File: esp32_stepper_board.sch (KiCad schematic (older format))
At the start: 35 parts, among them J1 Micro_SD_Card, J10 Endstop C/Z, J11 Aux1_I2C, J12 IO0_IO2_JP, J2 Aux2_GPIO, J3 DC_PWR, J4 Servo, J5 Stepper A/X, J6 Stepper B/Y, J7 Stepper C/Y, J8 Endstop A/X, J9 Endstop B/Y, SW1 Rotary_Encoder_Switch, U1 LM1117-5.0, U2 STEPSTICK, U3 ESP-DEVKITC, U4 STEPSTICK, U5 STEPSTICK, U6 OLED_I2C, U7 PCF8574

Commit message: Test board and components
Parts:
- removed C1: 100n, Capacitors_SMD:C_0805, symbol C
- removed J1: Micro_SD_Card, Connect:microSD_Card_Receptacle_Wuerth_693072010801, symbol Micro_SD_Card
- removed R2, R3, R4, R5, R6: 10k, Resistors_SMD:R_0805, symbol R
- removed SW1: Rotary_Encoder_Switch, symbol Rotary_Encoder_Switch
- added SW1: SW_DIP_x01, custom:SlideSw, symbol SW_DIP_x01
- added U3: lc_tech_sd_module, custom:lc_tech_sd_module, symbol lc_tech_sd_module
- added U7: rotary_enc_module, custom:ky-040-rotary-encoder-module, symbol rotary_enc_module
- C1: renamed from C2; footprint (none) -> Capacitors_ThroughHole:CP_Radial_D8.0mm_P2.50mm
- C2: renamed from C3; footprint (none) -> Capacitors_ThroughHole:CP_Radial_D8.0mm_P2.50mm
- C3: renamed from C4; footprint Capacitors_SMD:CP_Elec_6.3x7.7 -> custom:C_Radial_lying_flat_D8_L11_P2.5
- C4: renamed from C5; footprint Capacitors_SMD:CP_Elec_6.3x7.7 -> custom:C_Radial_lying_flat_D8_L11_P2.5
- C5: renamed from C6; footprint Capacitors_SMD:CP_Elec_6.3x7.7 -> custom:C_Radial_lying_flat_D8_L11_P2.5
- C6: renamed from C7; footprint Capacitors_SMD:C_0805 -> Capacitors_ThroughHole:C_Disc_D4.3mm_W1.9mm_P5.00mm
- J11: renamed from J12; footprint (none) -> Pin_Headers:Pin_Header_Straight_1x02_Pitch2.54mm
- R1: footprint Resistors_SMD:R_0805 -> Resistors_ThroughHole:R_Axial_DIN0204_L3.6mm_D1.6mm_P1.90mm_Vertical
- R2: renamed from R7; footprint Resistors_SMD:R_0805 -> Resistors_ThroughHole:R_Axial_DIN0204_L3.6mm_D1.6mm_P1.90mm_Vertical
- R3: renamed from R8; footprint Resistors_SMD:R_0805 -> Resistors_ThroughHole:R_Axial_DIN0204_L3.6mm_D1.6mm_P1.90mm_Vertical
- U1: footprint (none) -> TO_SOT_Packages_THT:TO-220-3_Vertical
- U4: renamed from U3; footprint (none) -> custom:DEVKITC
- U8: renamed from U6; footprint (none) -> custom:ssd1306_oled_0.96in
- U9: renamed from U7; footprint Housings_SOIC:SOIC-16_3.9x9.9mm_Pitch1.27mm -> Housings_DIP:DIP-16_W7.62mm
- renumbered J2 to J1, J11 to J10, J3 to J2, J4 to J3, J5 to J4, J6 to J5, J7 to J6, J8 to J7, J9 to J8, J10 to J9, U4 to U5, U5 to U6
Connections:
- net 12v: now also SW1.2; no longer J2.1
- net 3v3: now also U3.1 (3v3), U7.4 (Vin)
- net GND: now also U3.6 (GND), U7.5 (GND)
- net RENC_CLK: now also U7.1 (CLK)
- net RENC_DT: now also U7.2 (DT)
- net SD_MISO: now also U3.5 (MISO)
- net SD_MOSI: now also U3.3 (MOSI)
- net SD_SCK: now also U3.4 (CLK); no longer R1.2
- net ~RENC_SW: now also U7.3 (SW)
- new net: R1.2, U3.2 (CS)
- new net Vin: J2.1, SW1.1
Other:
- moved on the sheet: C1, C2, R1, U1, U4

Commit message: fix silk screen label for c/z stepper
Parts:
- J6: value Stepper C/Y -> Stepper C/Z
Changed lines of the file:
@@
 P 3150 10450
 F 0 "J6" H 3150 10650 50  0000 C CNN
-F 1 "Stepper C/Y" V 3250 10400 50  0000 C CNN
+F 1 "Stepper C/Z" V 3250 10400 50  0000 C CNN
 F 2 "Connectors_JST:JST_PH_B4B-PH-K_04x2.00mm_Straight" H 3150 10450 50  0001 C CNN
 F 3 "" H 3150 10450 50  0001 C CNN

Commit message: Fixed devkit footprint and rerouted board
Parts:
- removed J1: Aux2_GPIO, Connectors_JST:JST_PH_B12B-PH-K_12x2.00mm_Straight, symbol Conn_02x06_Odd_Even
- added J1: AUX_2A_GPIO_LN, Connectors_JST:JST_PH_B6B-PH-K_06x2.00mm_Straight, symbol Conn_01x06
- added J12: PWRSEL_2A, Pin_Headers:Pin_Header_Straight_1x03_Pitch2.54mm, symbol Conn_01x03
- added J13: AUX_2B_GPIO_HN, Connectors_JST:JST_PH_B6B-PH-K_06x2.00mm_Straight, symbol Conn_01x06
- added J14: PWRSEL_2B, Pin_Headers:Pin_Header_Straight_1x03_Pitch2.54mm, symbol Conn_01x03
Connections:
- net labels added: PWR1, PWR2
- wire segments 178 -> 184
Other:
- moved on the sheet: J10, J11, J2
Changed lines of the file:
@@
 LIBS:valves
 LIBS:custom
-LIBS:custom_parts
 LIBS:esp32_stepper_board-cache
 EELAYER 25 0
@@
 L Jack-DC J2
 U 1 1 5A64C62C
-P 7800 10300
-F 0 "J2" H 7800 10510 50  0000 C CNN
-F 1 "DC_PWR" H 7800 10125 50  0000 C CNN
-F 2 "Connect:BARREL_JACK" H 7850 10260 50  0001 C CNN
-F 3 "" H 7850 10260 50  0001 C CNN
-	1    7800 10300
-	1    0    0    -1
-$EndComp
-Text Label 8450 10400 2    60   ~ 0
-GND
-Text Label 8450 10200 2    60   ~ 0
+P 8150 10300
+F 0 "J2" H 8150 10510 50  0000 C CNN
+F 1 "DC_PWR" H 8150 10125 50  0000 C CNN
+F 2 "Connect:BARREL_JACK" H 8200 10260 50  0001 C CNN
+F 3 "" H 8200 10260 50  0001 C CNN
+	1    8150 10300
+	1    0    0    -1
+$EndComp
+Text Label 8800 10400 2    60   ~ 0
+GND
+Text Label 8800 10200 2    60   ~ 0
 Vin
 $Comp
@@
 Text Label 5000 3350 0    60   ~ 0
 RENC_DT
-$Comp
-L Conn_02x06_Odd_Even J1
-U 1 1 5AA0C7C0
-P 6500 10150
-F 0 "J1" H 6550 10450 50  0000 C CNN
-F 1 "Aux2_GPIO" H 6550 9750 50  0000 C CNN
-F 2 "Connectors_JST:JST_PH_B12B-PH-K_12x2.00mm_Straight" H 6500 10150 50  0001 C CNN
-F 3 "" H 6500 10150 50  0001 C CNN
-	1    6500 10150
-	1    0    0    -1
-$EndComp
-Text Label 7200 10150 2    60   ~ 0
-GND
-Text Label 5900 10250 0    60   ~ 0
-GND
-Text Label 7200 10250 2    60   ~ 0
-3v3
-Text Label 5900 10150 0    60   ~ 0
+Text Label 7000 9850 3    60   ~ 0
+GND
+Text Label 7600 9850 3    60   ~ 0
+3v3
+Text Label 6550 9850 3    60   ~ 0
 5v
 Text Label 4200 6750 2    60   ~ 0
@@
 Text Label 4200 7450 2    60   ~ 0
 GPIO_EX7
-Text Label 5900 9950 0    60   ~ 0
+Text Label 5800 9850 3    60   ~ 0
 GPIO_EX0
-Text Label 7200 9950 2    60   ~ 0
+Text Label 5900 9850 3    60   ~ 0
 GPIO_EX1
-Text Label 5900 10050 0    60   ~ 0
+Text Label 6000 9850 3    60   ~ 0
 GPIO_EX2
-Text Label 7200 10050 2    60   ~ 0
+Text Label 6100 9850 3    60   ~ 0
 GPIO_EX3
-Text Label 5900 10350 0    60   ~ 0
+Text Label 7100 9850 3    60   ~ 0
 GPIO_EX4
-Text Label 7200 10350 2    60   ~ 0
+Text Label 7200 9850 3    60   ~ 0
 GPIO_EX5
-Text Label 5900 10450 0    60   ~ 0
+Text Label 7300 9850 3    60   ~ 0
 GPIO_EX6
-Text Label 7200 10450 2    60   ~ 0
+Text Label 7400 9850 3    60   ~ 0
 GPIO_EX7
 $Comp
 L Conn_01x04 J10
 U 1 1 5AA0F0CE
-P 5300 10450
-F 0 "J10" H 5300 10650 50  0000 C CNN
-F 1 "Aux1_I2C" V 5400 10400 50  0000 C CNN
-F 2 "Connectors_JST:JST_PH_B4B-PH-K_04x2.00mm_Straight" H 5300 10450 50  0001 C CNN
-F 3 "" H 5300 10450 50  0001 C CNN
-	1    5300 10450
-	0    1    1    0
-$EndComp
-Text Label 5400 9950 3    60   ~ 0
-GND
+P 5200 10450
+F 0 "J10" H 5200 10650 50  0000 C CNN
+F 1 "Aux1_I2C" V 5300 10400 50  0000 C CNN
+F 2 "Connectors_JST:JST_PH_B4B-PH-K_04x2.00mm_Straight" H 5200 10450 50  0001 C CNN
+F 3 "" H 5200 10450 50  0001 C CNN
+	1    5200 10450
+	0    1    1    0
+$EndComp
+Text Label 5300 9950 3    60   ~ 0
+GND
+Text Label 5100 9950 3    60   ~ 0
+3v3
 Text Label 5200 9950 3    60   ~ 0
-3v3
-Text Label 5300 9950 3    60   ~ 0
 SDA1
-Text Label 5100 9950 3    60   ~ 0
+Text Label 5000 9950 3    60   ~ 0
 SCL1
 $Comp
@@
 L Conn_01x02 J11
 U 1 1 5AA42D41
-P 8950 10450
-F 0 "J11" H 8950 10550 50  0000 C CNN
-F 1 "IO0_IO2_JP" V 9050 10400 50  0000 C CNN
-F 2 "Pin_Headers:Pin_Header_Straight_1x02_Pitch2.54mm" H 8950 10450 50  0001 C CNN
-F 3 "" H 8950 10450 50  0001 C CNN
-	1    8950 10450
-	0    1    1    0
-$EndComp
-Text Label 8850 9900 3    60   ~ 0
+P 9100 10450
+F 0 "J11" H 9100 10550 50  0000 C CNN
+F 1 "IO0_IO2_JP" V 9200 10400 50  0000 C CNN
+F 2 "Pin_Headers:Pin_Header_Straight_1x02_Pitch2.54mm" H 9100 10450 50  0001 C CNN
+F 3 "" H 9100 10450 50  0001 C CNN
+	1    9100 10450
+	0    1    1    0
+$EndComp
+Text Label 9000 9900 3    60   ~ 0
 IO0
-Text Label 8950 9900 3    60   ~ 0
+Text Label 9100 9900 3    60   ~ 0
 SD_MOSI
 $Comp
@@
 	3250 9950 3250 10250
 Wire Wire Line
-	8100 10400 8450 10400
-Wire Wire Line
-	8100 10200 8450 10200
+	8450 10400 8800 10400
+Wire Wire Line
+	8450 10200 8800 10200
 Wire Wire Line
 	6200 6950 5800 6950
@@
 	5500 2450 5000 2450
 Wire Wire Line
-	6300 9950 5900 9950
-Wire Wire Line
-	6800 9950 7200 9950
-Wire Wire Line
-	6300 10050 5900 10050
-Wire Wire Line
-	6300 10150 5900 10150
-Wire Wire Line
-	6300 10250 5900 10250
-Wire Wire Line
-	6300 10350 5900 10350
-Wire Wire Line
-	6300 10450 5900 10450
-Wire Wire Line
-	6800 10050 7200 10050
-Wire Wire Line
-	6800 10150 7200 10150
-Wire Wire Line
-	6800 10250 7200 10250
-Wire Wire Line
-	6800 10350 7200 10350
-Wire Wire Line
-	6800 10450 7200 10450
-Wire Wire Line
-	5400 10250 5400 9950
-Wire Wire Line
 	5300 10250 5300 9950
 Wire Wire Line
@@
 Wire Wire Line
 	5100 10250 5100 9950
+Wire Wire Line
+	5000 10250 5000 9950
 Wire Notes Line
 	10150 5600 10150 7200
@@
 	7350 3650 7900 3650
 Wire Wire Line
-	8950 9900 8950 10250
-Wire Wire Line
-	8850 9900 8850 10250
+	9100 9900 9100 10250
+Wire Wire Line
+	9000 9900 9000 10250
 Wire Notes Line
 	9400 10750 9400 9600
@@
 Text Label 4300 2000 2    60   ~ 0
 5v
+$Comp
+L Conn_01x06 J1
+U 1 1 5AB7CE2D
+P 5900 10450
+F 0 "J1" H 5900 10750 50  0000 C CNN
+F 1 "AUX_2A_GPIO_LN" V 6000 10400 50  0000 C CNN
+F 2 "Connectors_JST:JST_PH_B6B-PH-K_06x2.00mm_Straight" H 5900 10450 50  0001 C CNN
+F 3 "" H 5900 10450 50  0001 C CNN
+	1    5900 10450
+	0    1    1    0
+$EndComp
+$Comp
+L Conn_01x06 J13
+U 1 1 5AB7CF32
+P 7200 10450
+F 0 "J13" H 7200 10750 50  0000 C CNN
+F 1 "AUX_2B_GPIO_HN" V 7300 10400 50  0000 C CNN
+F 2 "Connectors_JST:JST_PH_B6B-PH-K_06x2.00mm_Straight" H 7200 10450 50  0001 C CNN
+F 3 "" H 7200 10450 50  0001 C CNN
+	1    7200 10450
+	0    1    1    0
+$EndComp
+Wire Wire Line
+	5600 9850 5600 10250
+Wire Wire Line
+	5700 9850 5700 10250
+Wire Wire Line
+	5800 9850 5800 10250
+Wire Wire Line
+	5900 9850 5900 10250
+Wire Wire Line
+	6000 9850 6000 10250
+Wire Wire Line
+	6100 9850 6100 10250
+Wire Wire Line
+	6900 9850 6900 10250
+Wire Wire Line
+	7000 9850 7000 10250
+Wire Wire Line
+	7100 9850 7100 10250
+Wire Wire Line
+	7200 9850 7200 10250
+Wire Wire Line
+	7300 9850 7300 10250
+Wire Wire Line
+	7400 9850 7400 10250
+Text Label 5600 9850 3    60   ~ 0
+PWR1
+Text Label 5700 9850 3    60   ~ 0
+GND
+Text Label 6900 9850 3    60   ~ 0
+PWR2
+$Comp
+L Conn_01x03 J12
+U 1 1 5AB7F4B6
+P 6450 10450
+F 0 "J12" H 6450 10650 50  0000 C CNN
+F 1 "PWRSEL_2A" V 6550 10450 50  0000 C CNN
+F 2 "Pin_Headers:Pin_Header_Straight_1x03_Pitch2.54mm" H 6450 10450 50  0001 C CNN
+F 3 "" H 6450 10450 50  0001 C CNN
+	1    6450 10450
+	0    1    1    0
+$EndComp
+$Comp
+L Conn_01x03 J14
+U 1 1 5AB7F53B
+P 7700 10450
+F 0 "J14" H 7700 10650 50  0000 C CNN
+F 1 "PWRSEL_2B" V 7800 10500 50  0000 C CNN
+F 2 "Pin_Headers:Pin_Header_Straight_1x03_Pitch2.54mm" H 7700 10450 50  0001 C CNN
+F 3 "" H 7700 10450 50  0001 C CNN
+	1    7700 10450
+	0    1    1    0
+$EndComp
+Wire Wire Line
+	6450 10250 6450 9850
+Wire Wire Line
+	6350 10250 6350 9850
+Wire Wire Line
+	6550 10250 6550 9850
+Wire Wire Line
+	7600 10250 7600 9850
+Wire Wire Line
+	7700 9850 7700 10250
+Wire Wire Line
+	7800 10250 7800 9850
+Text Label 6350 9850 3    60   ~ 0
+3v3
+Text Label 7800 9850 3    60   ~ 0
+5v
+Text Label 7700 9850 3    60   ~ 0
+PWR2
+Text Label 6450 9850 3    60   ~ 0
+PWR1
 $EndSCHEMATC

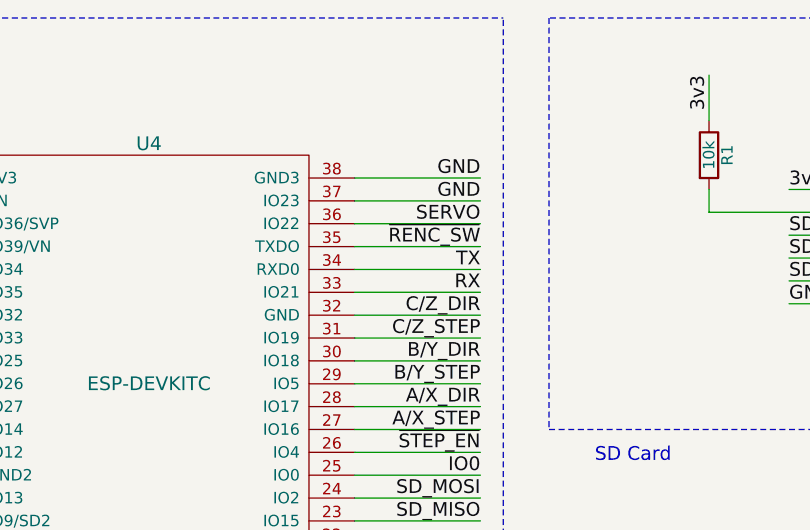
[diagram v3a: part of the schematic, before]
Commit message: Fixed devkitc footprint silk, rotated devkitc footprint, fix stepper pwr track width, c_step pin on IO23 (moved from gnd), moved renc_sw from tx.
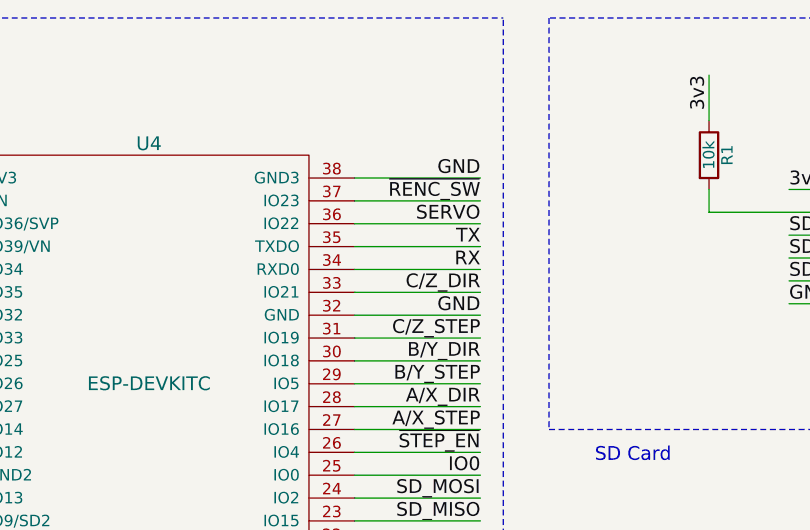
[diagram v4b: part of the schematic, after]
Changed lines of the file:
@@
 Text Label 7900 2150 2    60   ~ 0
 GND
-Text Label 7900 2250 2    60   ~ 0
+Text Label 7900 2750 2    60   ~ 0
 GND
 Text Label 5000 2150 0    60   ~ 0
@@
 Text Label 7900 3350 2    60   ~ 0
 ~STEP_EN
+Text Label 7900 2450 2    60   ~ 0
+TX
 Text Label 7900 2550 2    60   ~ 0
-TX
-Text Label 7900 2650 2    60   ~ 0
 RX
 Text Label 7900 3150 2    60   ~ 0
@@
 Text Label 7900 2850 2    60   ~ 0
 C/Z_STEP
-Text Label 7900 2750 2    60   ~ 0
+Text Label 7900 2650 2    60   ~ 0
 C/Z_DIR
 Text Label 7900 2350 2    60   ~ 0
@@
 Text Label 5000 2550 0    60   ~ 0
 ~ES_C/Z
-Text Label 7900 2450 2    60   ~ 0
+Text Label 7900 2250 2    60   ~ 0
 ~RENC_SW
 Text Label 5000 3550 0    60   ~ 0
